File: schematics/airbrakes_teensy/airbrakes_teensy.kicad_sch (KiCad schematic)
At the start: 9 parts, among them U6 XL1509-3.3

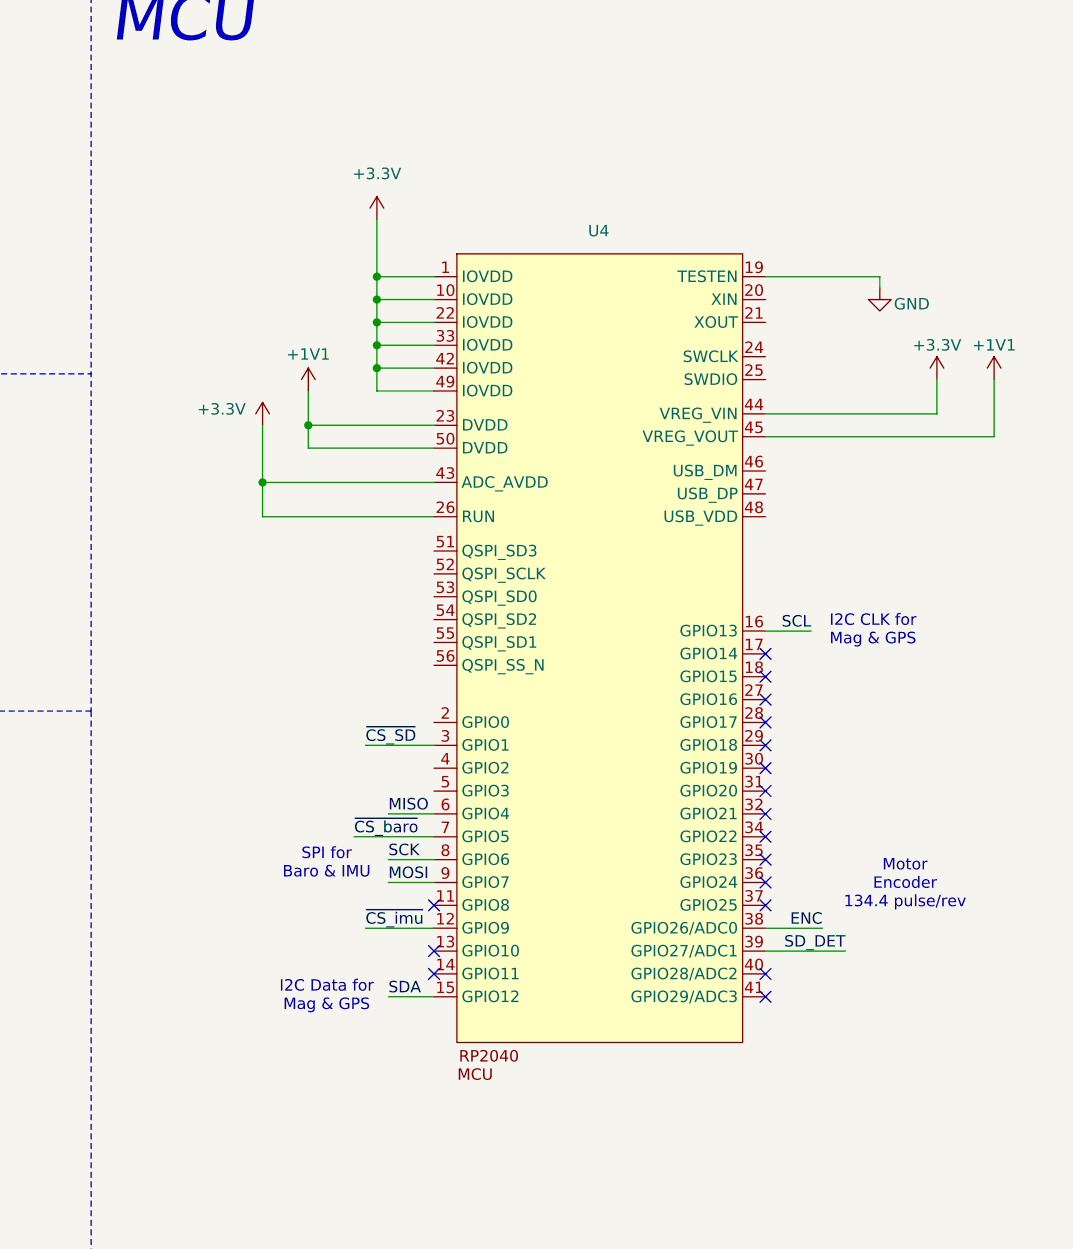
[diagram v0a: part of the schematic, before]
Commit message: Add teensy to schematic with some data connections
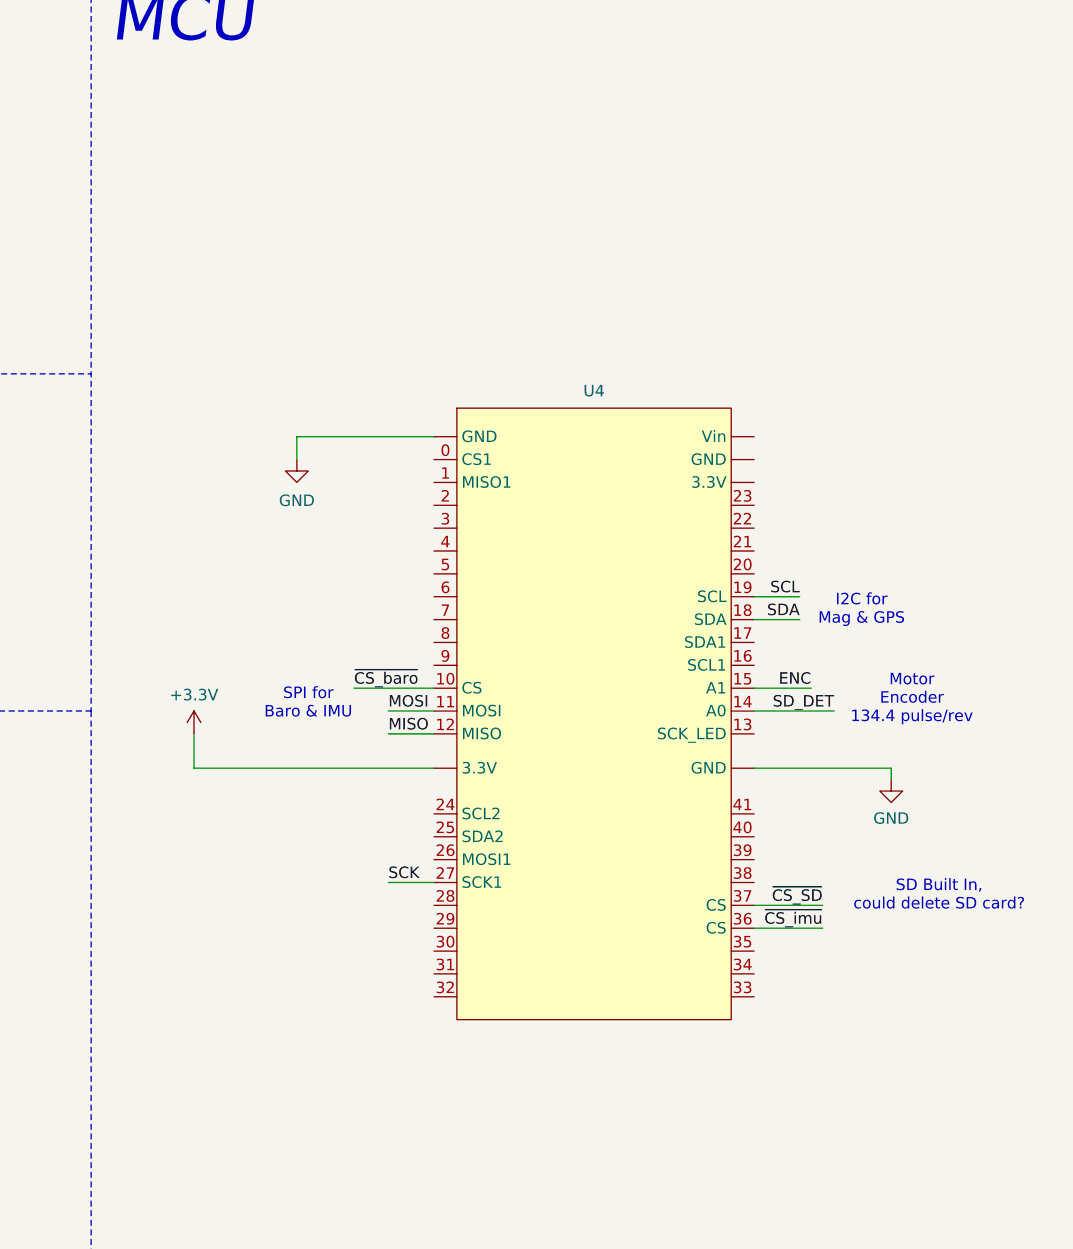
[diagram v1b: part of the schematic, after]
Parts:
- removed U4: (no value), symbol airbrakes_1:RP2040
- added U4: (no value), symbol airbrakes_1:Teensy_4.1
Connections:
- net +3.3V: now also U4. (GND)
- net ENC: now also U4.15 (A1)
- net GND: now also U4. (GND)
- net MISO: now also U4.12 (MISO)
- net MOSI: now also U4.11 (MOSI)
- net SCK: now also U4.27 (SCK1)
- net SCL: now also U4.19 (SCL)
- net SDA: now also U4.18 (SDA)
- net SD_DET: now also U4.14 (A0)
- net ~{CS_SD}: now also U4.37 (CS)
- net ~{CS_baro}: now also U4.10 (CS)
- net ~{CS_imu}: now also U4.36 (CS)
- no-connect marks 28 -> 11
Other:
- note added: "I2C for Mag & GPS"
- note added: "SD Built In, could delete SD card?"
- note removed: "I2C CLK for Mag & GPS"
- note removed: "I2C Data for Mag & GPS"

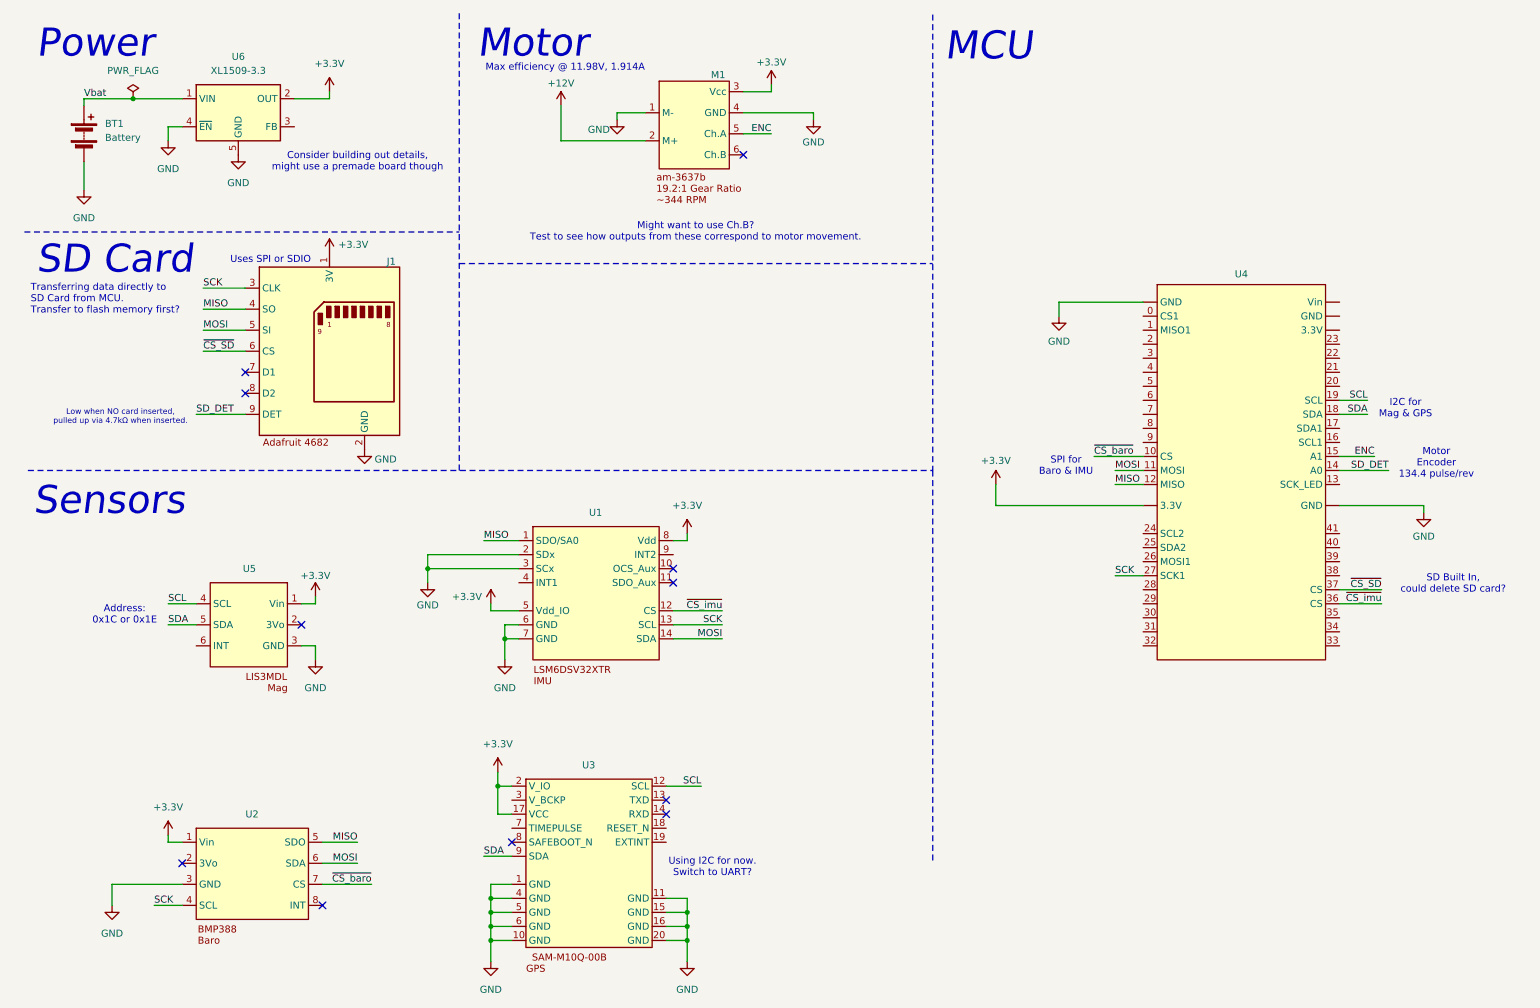
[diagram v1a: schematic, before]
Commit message: add limit switches, connect interrupts
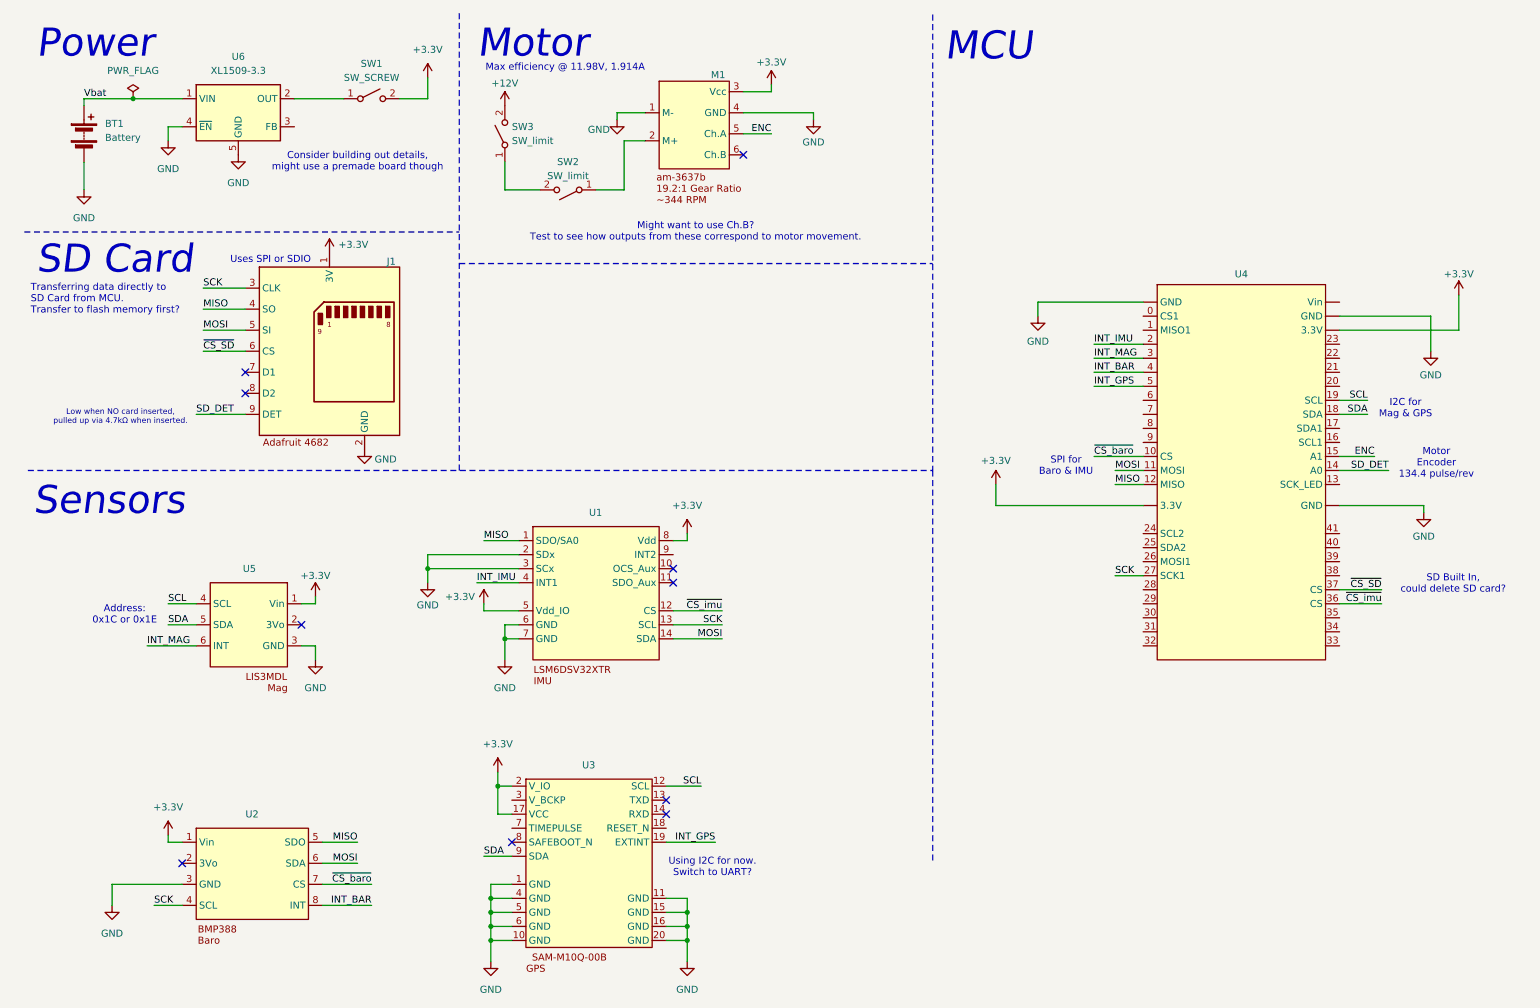
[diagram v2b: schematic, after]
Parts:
- added SW1: SW_SCREW, Button_Switch_SMD:Nidec_Copal_CAS-120A, symbol Switch:SW_SPST
- added SW2, SW3: SW_limit, symbol Switch:SW_SPST
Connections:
- net +12V: now also SW3.2 (B); no longer M1.2 (M+)
- net +3.3V: now also SW1.2 (B); no longer U6.2 (OUT)
- net INT_GPS: now reaches U3.19 (EXTINT)
- net INT_GPS: now also U4.5
- net INT_IMU: now reaches U1.4 (INT1)
- net INT_IMU: now also U4.2
- net INT_MAG: now reaches U5.6 (INT)
- net INT_MAG: now also U4.3
- net INT_BAR: now reaches U2.8 (INT)
- net INT_BAR: now also U4.4
- new net: M1.2 (M+), SW2.1 (A)
- new net: SW1.1 (A), U6.2 (OUT)
- new net: SW2.2 (B), SW3.1 (A)
- no-connect marks 11 -> 10

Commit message: add flash mem (adafruit 5643)
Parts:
- added U7: (no value), symbol airbrakes_1:Adafruit_5643
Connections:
- net +3.3V: now also U7.1 (Vin)
- net GND: now also U7.3 (GND)
- net SCK: now also U4.13 (SCK_LED); no longer U4.27 (SCK1)
- net ~{CS_flash}: now reaches U4.0 (CS1)
- net ~{CS_flash}: now also U7.7 (CS)
- net MISO1: now reaches U4.1 (MISO1)
- net MISO1: now also U7.5 (MISO)
- net MOSI1: now reaches U4.26 (MOSI1)
- net MOSI1: now also U7.6 (MOSI)
- new net SCK1: U4.27 (SCK1), U7.4 (SCK)
- no-connect marks 10 -> 11
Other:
- note added: "Flash"
- note added: "Flash on separate SPI bus."

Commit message: EOD oct-15
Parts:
- renumbered U4 to U1, U1 to U4
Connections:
- net INT_GPS: no longer names the net of U3.19 (EXTINT)
- net INT_GPS: no longer U1.5
- no-connect marks 11 -> 13
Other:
- note added: "Flash on separate SPI bus from sensors."
- note removed: "Flash on separate SPI bus."
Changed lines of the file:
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@@
 		)
 	)
-	(text "Flash on separate\nSPI bus."
+	(text "Flash on separate\nSPI bus from sensors."
 		(exclude_from_sim no)
 		(at 103.632 72.39 0)
@@
 	)
 	(no_connect
+		(at 128.27 162.56)
+	)
+	(no_connect
 		(at 62.23 123.19)
 	)
@@
 	)
 	(no_connect
+		(at 129.54 110.49)
+	)
+	(no_connect
 		(at 129.54 115.57)
 	)
@@
 	(polyline
 		(pts
-			(xy 176.53 12.7) (xy 176.53 95.25)
+			(xy 177.165 12.7) (xy 177.165 95.25)
 		)
 		(stroke
@@
 	(polyline
 		(pts
-			(xy 90.805 57.785) (xy 176.53 57.785)
+			(xy 90.805 57.785) (xy 177.165 57.785)
 		)
 		(stroke
@@
 	(wire
 		(pts
-			(xy 128.27 162.56) (xy 137.16 162.56)
-		)
-		(stroke
-			(width 0)
-			(type default)
-		)
-	)
-	(wire
-		(pts
 			(xy 142.24 30.48) (xy 154.94 30.48)
 		)
@@
 	(polyline
 		(pts
-			(xy 176.53 95.25) (xy 176.53 166.37)
+			(xy 177.165 95.25) (xy 177.165 166.37)
 		)
 		(stroke
@@
 	(wire
 		(pts
-			(xy 205.74 80.01) (xy 214.63 80.01)
-		)
-		(stroke
-			(width 0)
-			(type default)
-		)
-	)
-	(wire
-		(pts
 			(xy 142.24 34.29) (xy 147.32 34.29)
 		)
@@
 		)
 	)
-	(label "INT_GPS"
-		(at 137.16 162.56 180)
-		(effects
-			(font
-				(size 1.27 1.27)
-			)
-			(justify right bottom)
-		)
-	)
 	(label "MOSI"
 		(at 209.55 95.25 0)
@@
 		)
 	)
-	(label "INT_GPS"
-		(at 205.74 80.01 0)
-		(effects
-			(font
-				(size 1.27 1.27)
-			)
-			(justify left bottom)
-		)
-	)
 	(label "MOSI"
 		(at 72.39 166.37 180)
@@
 		(in_pos_files yes)
 		(dnp no)
-		(fields_autoplaced yes)
 		(property "Reference" "U3"
-			(at 114.2353 148.59 0)
+			(at 124.206 150.114 0)
 			(show_name no)
 			(do_not_autoplace no)
@@
 		(in_pos_files yes)
 		(dnp no)
-		(fields_autoplaced yes)
-		(property "Reference" "U1"
-			(at 115.4872 102.87 0)
+		(property "Reference" "U4"
+			(at 125.73 104.14 0)
 			(show_name no)
 			(do_not_autoplace no)
@@
 			(project "airbrakes_teensy"
 				(path "/4056183e-e49a-49da-b487-53d090193030"
-					(reference "U1")
+					(reference "U4")
 					(unit 1)
 				)
@@
 		(in_pos_files yes)
 		(dnp no)
-		(fields_autoplaced yes)
 		(property "Reference" "U7"
-			(at 159.512 66.294 0)
+			(at 159.004 66.294 0)
 			(show_name no)
 			(do_not_autoplace yes)
@@
 		(in_pos_files yes)
 		(dnp no)
-		(fields_autoplaced yes)
 		(property "Reference" "U5"
-			(at 52.806 113.03 0)
+			(at 58.42 114.3 0)
 			(show_name no)
 			(do_not_autoplace no)
@@
 		(in_pos_files yes)
 		(dnp no)
-		(fields_autoplaced yes)
 		(property "Reference" "U2"
-			(at 53.2844 157.48 0)
+			(at 61.722 159.004 0)
 			(show_name no)
 			(do_not_autoplace no)
@@
 		(dnp no)
 		(fields_autoplaced yes)
-		(property "Reference" "U4"
+		(property "Reference" "U1"
 			(at 232.41 59.69 0)
 			(show_name no)
@@
 			(project "airbrakes_teensy"
 				(path "/4056183e-e49a-49da-b487-53d090193030"
-					(reference "U4")
+					(reference "U1")
 					(unit 1)
 				)
@@
 		)
 		(property "Value" "GND"
-			(at 195.58 71.882 0)
+			(at 195.58 71.374 0)
 			(show_name no)
 			(do_not_autoplace no)
